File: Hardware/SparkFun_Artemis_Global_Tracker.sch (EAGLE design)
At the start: 144 parts, among them J1 IRIDIUM_9603N, J2 USB-C, J6 U.FL, J7 ANTENNA-GROUNDEDEDGE_SMA, J8 STANDOFFS_M2X0.4_STEEL_6MM, J9 STANDOFFS_M2X0.4_STEEL_6MM, Q1 5.8A/30V/35mΩ, Q2 20V/4.2A/52mΩ/1.4W, Q3 20V/4.2A/52mΩ/1.4W, Q4 600mA/40V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

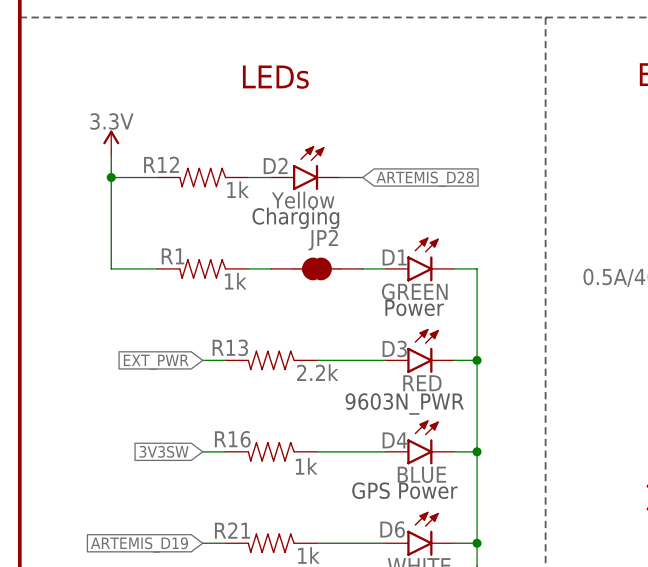
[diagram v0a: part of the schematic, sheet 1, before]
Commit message: silk updates and R1 to 330 for brighter green power led
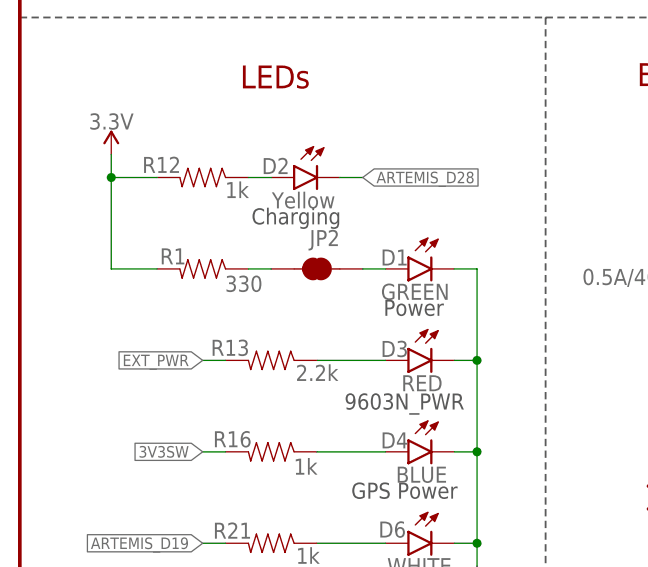
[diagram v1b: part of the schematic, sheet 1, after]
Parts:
- R1: value 1k -> 330; device SparkFun-Resistors:1KOHM-0603-1/10W-1% -> SparkFun-Resistors:330OHM-0603-1/10W-1%
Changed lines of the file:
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@@
 <part name="JP7" library="SparkFun-Aesthetics" deviceset="FIDUCIAL" device="1X2"/>
 <part name="JP13" library="SparkFun-Aesthetics" deviceset="FIDUCIAL" device="1X2"/>
-<part name="R1" library="SparkFun-Resistors" deviceset="1KOHM" device="-0603-1/10W-1%" value="1k"/>
+<part name="R1" library="SparkFun-Resistors" deviceset="330OHM" device="-0603-1/10W-1%" value="330"/>
 <part name="SUPPLY10" library="SparkFun-PowerSymbols" deviceset="3.3V" device=""/>
 <part name="D1" library="SparkFun-LED" deviceset="LED-GREEN" device="0603" value="GREEN"/>
@@
 <instance part="R1" gate="G$1" x="20.32" y="175.26" smashed="yes" rot="MR0">
 <attribute name="NAME" x="17.018" y="175.768" size="1.778" layer="95" font="vector" rot="MR0" align="bottom-center"/>
-<attribute name="VALUE" x="23.876" y="174.752" size="1.778" layer="96" font="vector" rot="MR0" align="top-center"/>
+<attribute name="VALUE" x="24.892" y="174.498" size="1.778" layer="96" font="vector" rot="MR0" align="top-center"/>
 </instance>
 <instance part="SUPPLY10" gate="G$1" x="10.16" y="187.96" smashed="yes" rot="MR0">

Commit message: backup battery charge resistor val and switch
-added pch mosfet to switch backup battery charging on and off via GPIO on artemis
-changed backup battery charge source to 3.3V rail, and changed charge resistor to 3.3K
-Moved Iridium module and artemis module down 0.1 inch to allow more clearance around sam-tech connector so epoxy is less likely to flow over/into nearby additional supercap pth pads.
-moved a few other components from 0603 to 0402 to make more room.
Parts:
- added Q6: 20V/4.2A/52mΩ/1.4W, SparkFun-DiscreteSemi:MOSFET_PCH-DMG2305UX-7
- added R19: 10K, SparkFun-Resistors:10KOHM-0402-1/10W-0.1%
- R1: device SparkFun-Resistors:330OHM-0603-1/10W-1% -> SparkFun-Resistors:330OHM-0402T-1/16W-5%
- R12, R16, R2, R21, R25, R29, R3: device SparkFun-Resistors:1KOHM-0603-1/10W-1% -> SparkFun-Resistors:1KOHM-0402T-1/16W-1%
- R13: value 2.2k -> 2.0K; device SparkFun-Resistors:2.2KOHM-0603-1/10W-1% -> SparkFun-Resistors:2.0KOHM-0402T-1/16W-1%
- R15: value 62KOHM-0603-1/10W-5% -> 3.3K; device SparkFun-Resistors:62KOHM-0603-1/10W-5% -> SparkFun-Resistors:3.3KOHM-0402T-1/16W-1%
- R28: value 2.0k -> 2.0K; device SparkFun-Resistors:2.0KOHM-0603-1/10W-5% -> SparkFun-Resistors:2.0KOHM-0402T-1/16W-1%
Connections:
- new net ARTEMIS_D44: Q6.G, R19.1, U7.(SDO4)~D44
- new net N$7: D5.A, Q6.D
- net 3.3V: now also Q6.S, R19.2
- net V_USB: no longer D5.A
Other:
- note added: "Back-Up Battery And charge control switch"
- note added: "R15 = (3.3 - (3.1 + 0.1)) / 30E-6 = ~3.3K"
- note removed: "Back-Up Battery"
- note removed: "R15 = (5 - (3.1 + 0.1)) / 30E-6 = ~60K"
- moved on the sheet: 3V3SW, B1, C12, C14, C15, C16, D5, J6, J7, Q2, R15, R17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

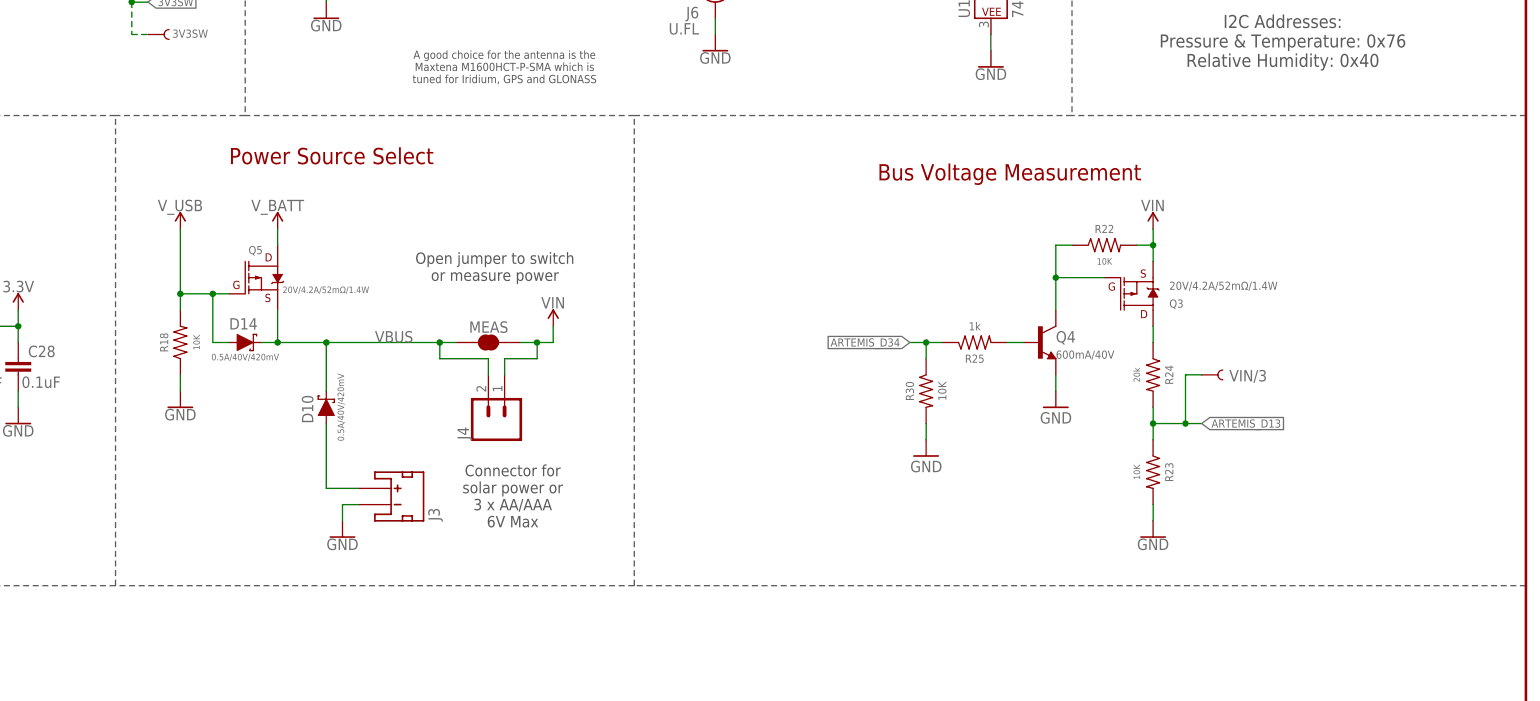
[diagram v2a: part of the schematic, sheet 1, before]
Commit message: Reverted back to battery input diode
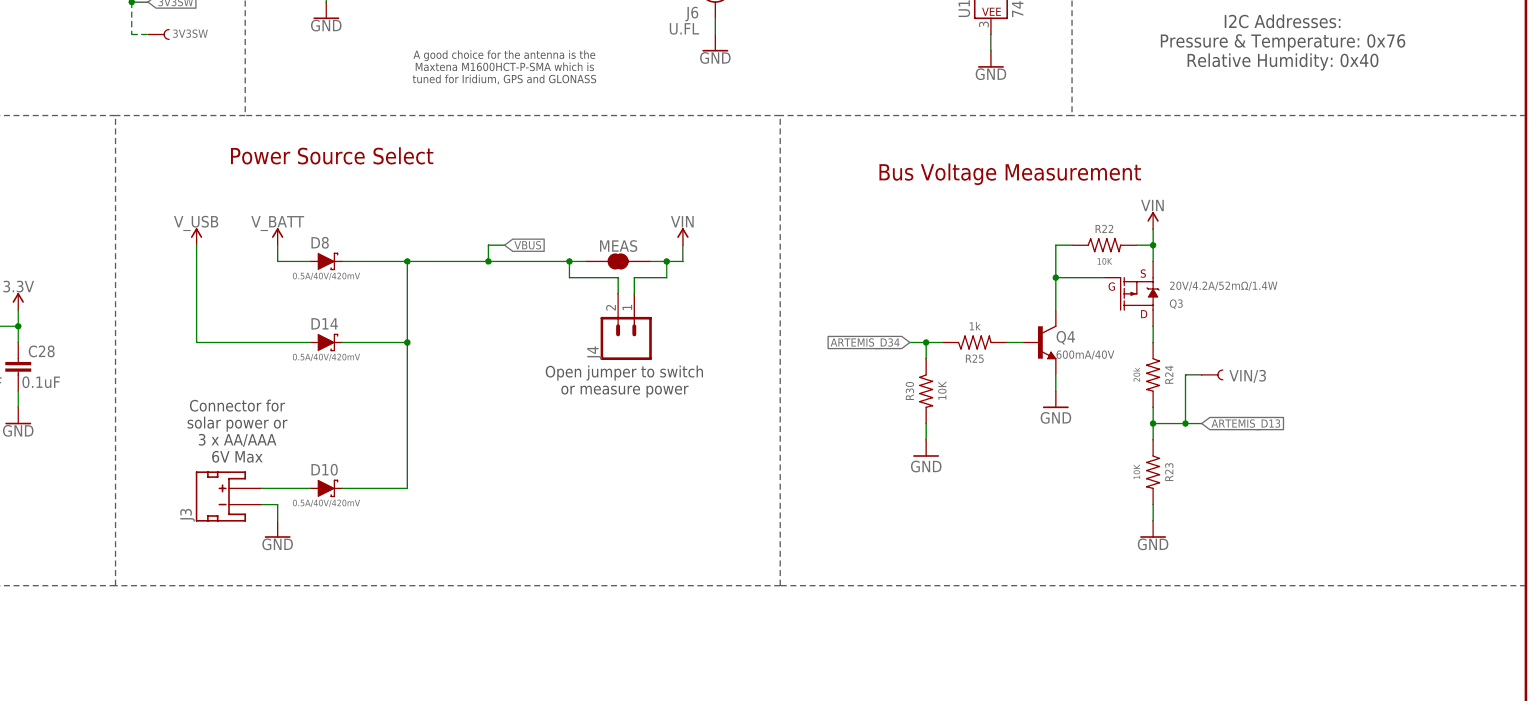
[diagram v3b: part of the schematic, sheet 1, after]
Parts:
- removed Q5: 20V/4.2A/52mΩ/1.4W, SparkFun-DiscreteSemi:MOSFET_PCH-DMG2305UX-7
- removed R18: 10K, SparkFun-Resistors:10KOHM-0402-1/10W-0.1%
- added D8: 0.5A/40V/420mV, SparkFun-DiscreteSemi:DIODE-SCHOTTKY-PMEG4005EJ
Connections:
- net GND: no longer R18.1
- net VBUS: now also D8.C; no longer Q5.S
- net V_BATT: now also D8.A; no longer Q5.D
- net V_USB: no longer Q5.G, R18.2
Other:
- moved on the sheet: D10, D14, J3, J4, MEAS

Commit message: Moved all 0.1uF caps to higher spec'd part
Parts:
- C13, C28, C7: device SparkFun-Capacitors:0.1UF-0402T-16V-10% -> SparkFun-Capacitors:0.1UF-0603-25V-5%
- C20: device SparkFun-Capacitors:0.1UF-0603-25V-(+80/-20%) -> SparkFun-Capacitors:0.1UF-0603-25V-5%
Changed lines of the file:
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@@
 <part name="B1" library="SparkFun-Batteries" deviceset="ML414H_IV01E_BATTERY" device=""/>
 <part name="L1" library="SparkFun-Coils" deviceset="2.2μH_SHIELDED_INDUCTOR" device="" value="2.2uH"/>
-<part name="C13" library="SparkFun-Capacitors" deviceset="0.1UF" device="-0402T-16V-10%" value="0.1uF"/>
+<part name="C13" library="SparkFun-Capacitors" deviceset="0.1UF" device="-0603-25V-5%" value="0.1uF"/>
 <part name="JP2" library="SparkFun-Jumpers" deviceset="JUMPER-SMT_2_NC_TRACE" device="_SILK" package3d_urn="urn:adsk.eagle:package:39281/1"/>
 <part name="SUPPLY20" library="SparkFun-PowerSymbols" deviceset="3.3V" device=""/>
@@
 <part name="C19" library="SparkFun-Capacitors" deviceset="15PF" device="-0603-50V-5%" value="15pF"/>
 <part name="GND35" library="SparkFun-PowerSymbols" deviceset="GND" device=""/>
-<part name="C20" library="SparkFun-Capacitors" deviceset="0.1UF" device="-0603-25V-(+80/-20%)" value="0.1uF"/>
+<part name="C20" library="SparkFun-Capacitors" deviceset="0.1UF" device="-0603-25V-5%" value="0.1uF"/>
 <part name="C22" library="SparkFun-Capacitors" deviceset="10UF" device="-0603-6.3V-20%" value="10uF"/>
 <part name="C23" library="SparkFun-Capacitors" deviceset="1.0UF" device="-0603-16V-10%" value="1.0uF"/>
@@
 <part name="C25" library="SparkFun-Capacitors" deviceset="22UF" device="-0603-6.3V-20%" value="22uF"/>
 <part name="C27" library="SparkFun-Capacitors" deviceset="1.0UF" device="-0603-16V-10%" value="1.0uF"/>
-<part name="C28" library="SparkFun-Capacitors" deviceset="0.1UF" device="-0402T-16V-10%" value="0.1uF"/>
+<part name="C28" library="SparkFun-Capacitors" deviceset="0.1UF" device="-0603-25V-5%" value="0.1uF"/>
 <part name="SUPPLY32" library="SparkFun-PowerSymbols" deviceset="3.3V" device=""/>
 <part name="R21" library="SparkFun-Resistors" deviceset="1KOHM" device="-0402T-1/16W-1%" value="1k"/>
@@
 <part name="D13" library="SparkFun-LED" deviceset="LED-YELLOW" device="0603" value="Yellow"/>
 <part name="R2" library="SparkFun-Resistors" deviceset="1KOHM" device="-0402T-1/16W-1%" value="1k"/>
-<part name="C7" library="SparkFun-Capacitors" deviceset="0.1UF" device="-0402T-16V-10%" value="0.1uF"/>
+<part name="C7" library="SparkFun-Capacitors" deviceset="0.1UF" device="-0603-25V-5%" value="0.1uF"/>
 <part name="R3" library="SparkFun-Resistors" deviceset="1KOHM" device="-0402T-1/16W-1%" value="1k"/>
 <part name="D7" library="SparkFun-LED" deviceset="LED-GREEN" device="0603" value="GREEN"/>

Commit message: Moved all 1.0uF caps to higher spec'd part
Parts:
- C23, C24, C27: device SparkFun-Capacitors:1.0UF-0603-16V-10% -> SparkFun-Capacitors:1.0UF-0603-16V-10%-X7R
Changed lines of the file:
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@@
 <part name="C20" library="SparkFun-Capacitors" deviceset="0.1UF" device="-0603-25V-5%" value="0.1uF"/>
 <part name="C22" library="SparkFun-Capacitors" deviceset="10UF" device="-0603-6.3V-20%" value="10uF"/>
-<part name="C23" library="SparkFun-Capacitors" deviceset="1.0UF" device="-0603-16V-10%" value="1.0uF"/>
+<part name="C23" library="SparkFun-Capacitors" deviceset="1.0UF" device="-0603-16V-10%-X7R" value="1.0uF"/>
 <part name="SUPPLY9" library="SparkFun-PowerSymbols" deviceset="3.3V" device=""/>
 <part name="SUPPLY21" library="SparkFun-PowerSymbols" deviceset="3.3V" device=""/>
@@
 <part name="C21" library="SparkFun-Capacitors" deviceset="22UF" device="-0805-16V-20%" value="22uF"/>
 <part name="C25" library="SparkFun-Capacitors" deviceset="22UF" device="-0603-6.3V-20%" value="22uF"/>
-<part name="C27" library="SparkFun-Capacitors" deviceset="1.0UF" device="-0603-16V-10%" value="1.0uF"/>
+<part name="C27" library="SparkFun-Capacitors" deviceset="1.0UF" device="-0603-16V-10%-X7R" value="1.0uF"/>
 <part name="C28" library="SparkFun-Capacitors" deviceset="0.1UF" device="-0603-25V-5%" value="0.1uF"/>
 <part name="SUPPLY32" library="SparkFun-PowerSymbols" deviceset="3.3V" device=""/>
@@
 <part name="JP10" library="SparkFun-Hardware" deviceset="STAND-OFF" device=""/>
 <part name="JP9" library="SparkFun-Hardware" deviceset="STAND-OFF" device=""/>
-<part name="C24" library="SparkFun-Capacitors" deviceset="1.0UF" device="-0603-16V-10%" value="1.0uF"/>
+<part name="C24" library="SparkFun-Capacitors" deviceset="1.0UF" device="-0603-16V-10%-X7R" value="1.0uF"/>
 <part name="SUPPLY17" library="SparkFun-PowerSymbols" deviceset="3.3V" device=""/>
 <part name="GND37" library="SparkFun-PowerSymbols" deviceset="GND" device=""/>

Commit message: Moved C25 to 0805 higher voltage rating
-to decrease BOM diversity
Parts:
- C25: device SparkFun-Capacitors:22UF-0603-6.3V-20% -> SparkFun-Capacitors:22UF-0805-16V-20%
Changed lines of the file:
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@@
 <part name="U7" library="SparkFun-IC-Microcontroller" deviceset="ARTEMIS_MODULE" device="SMD"/>
 <part name="C21" library="SparkFun-Capacitors" deviceset="22UF" device="-0805-16V-20%" value="22uF"/>
-<part name="C25" library="SparkFun-Capacitors" deviceset="22UF" device="-0603-6.3V-20%" value="22uF"/>
+<part name="C25" library="SparkFun-Capacitors" deviceset="22UF" device="-0805-16V-20%" value="22uF"/>
 <part name="C27" library="SparkFun-Capacitors" deviceset="1.0UF" device="-0603-16V-10%-X7R" value="1.0uF"/>
 <part name="C28" library="SparkFun-Capacitors" deviceset="0.1UF" device="-0603-25V-5%" value="0.1uF"/>

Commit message: Routed 8 more Artemis GPIOs to PTH headers
-routed AD32, D43, D42, AD31, AD29, AD11, D15 and AD12 to 0.1" PTH headers on upper right edge of board.
-removed full size sparkfun logo, added large flame.
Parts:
- added J10, J11: (no value), SparkFun-Connectors:CONN_041X04_NO_SILK_NO_POP
- LOGO2: value SFE_LOGO_NAME_FLAME.1_INCH -> SFE_LOGO_FLAME.3_INCH; device SparkFun-Aesthetics:SFE_LOGO_NAME_FLAME.1_INCH -> SparkFun-Aesthetics:SFE_LOGO_FLAME.3_INCH
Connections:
- new net ARTEMIS_AD11: J11.3, U7.~AD11(PDMDATA)
- new net ARTEMIS_AD12: J11.1, U7.~AD12(PDMCLK/TX1)
- new net ARTEMIS_AD29: J11.4, U7.~AD29(PDMDATA)
- new net ARTEMIS_AD31: J10.1, U7.~AD31(SCCCLK)
- new net ARTEMIS_AD32: J10.4, U7.~AD32(SCCIO)
- new net ARTEMIS_D15: J11.2, U7.(ADCD1N/RX1/PDMDATA)D15
- new net ARTEMIS_D42: J10.2, U7.(SCL3/SCK3/TX1)~D42
- new net ARTEMIS_D43: J10.3, U7.(SDA3/SDI3/RX1)~D43
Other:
- moved on the sheet: C18, C19, C24, I2C, QWIIC, X1

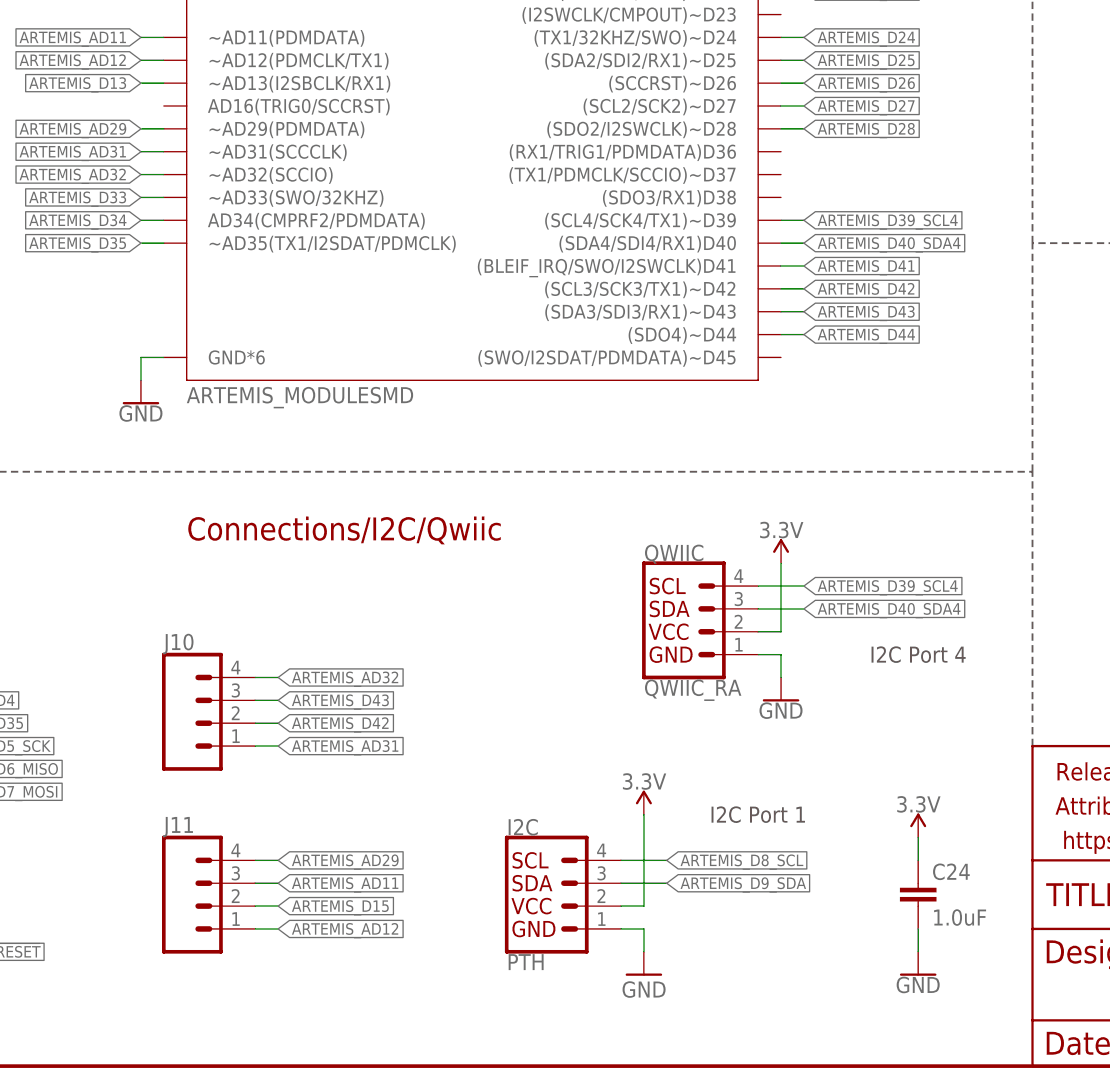
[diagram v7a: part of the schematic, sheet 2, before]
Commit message: Broke out D37 to bottom right corner PTH header
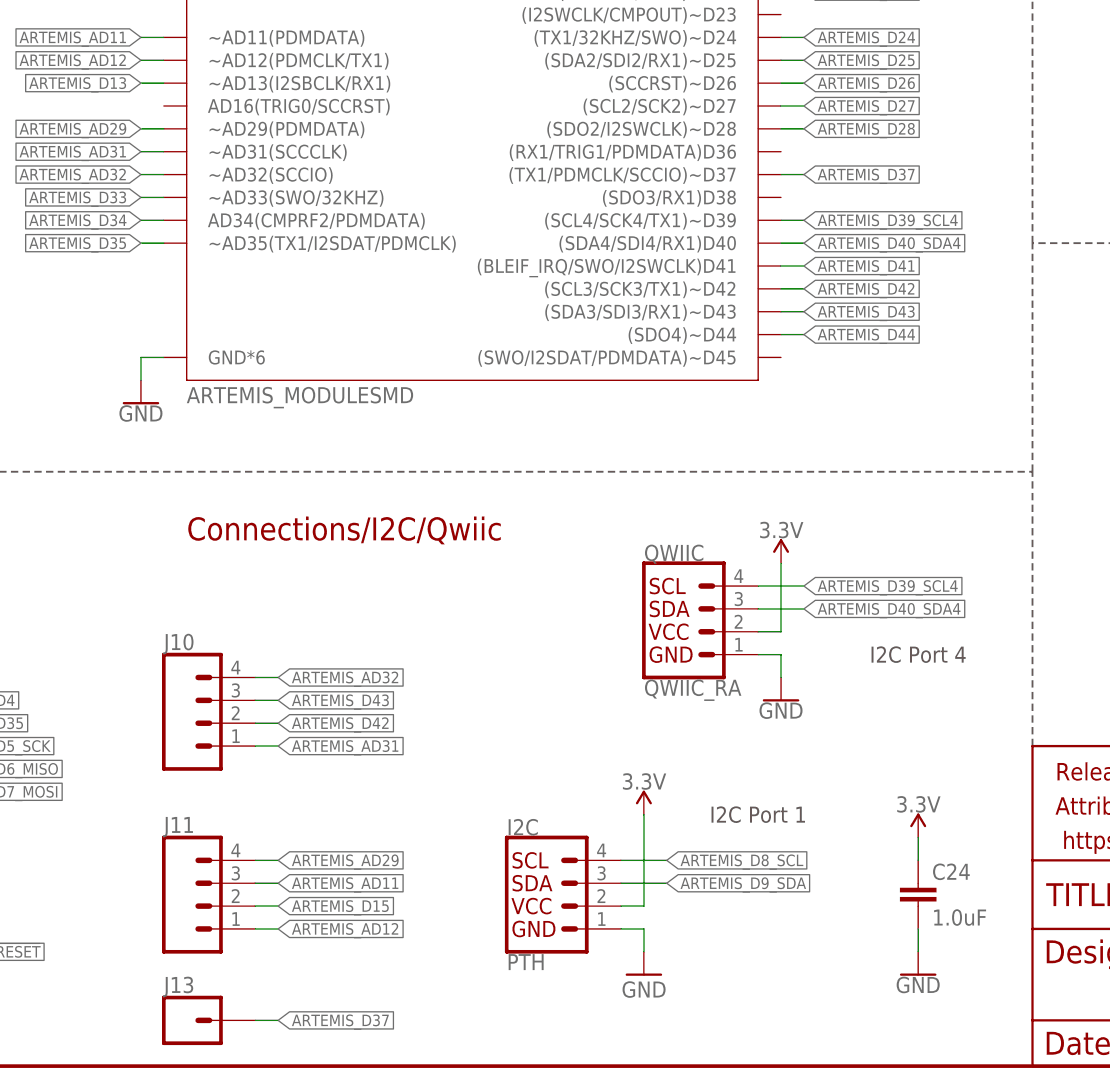
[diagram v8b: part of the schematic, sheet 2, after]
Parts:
- added J13: (no value), SparkFun-Connectors:CONN_01PTH_NO_SILK_YES_STOP
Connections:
- new net ARTEMIS_D37: J13.1, U7.(TX1/PDMCLK/SCCIO)~D37
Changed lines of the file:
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@@
 <part name="J11" library="SparkFun-Connectors" deviceset="CONN_04" device="1X04_NO_SILK_NO_POP"/>
 <part name="LOGO2" library="SparkFun-Aesthetics" deviceset="SFE_LOGO_FLAME" device=".3_INCH" value="SFE_LOGO_FLAME.3_INCH"/>
+<part name="J13" library="SparkFun-Connectors" deviceset="CONN_01" device="PTH_NO_SILK_YES_STOP"/>
 </parts>
 <sheets>
@@
 <attribute name="NAME" x="50.8" y="25.908" size="1.778" layer="95" font="vector"/>
 </instance>
+<instance part="J13" gate="G$1" x="53.34" y="5.08" smashed="yes">
+<attribute name="VALUE" x="50.8" y="0.254" size="1.778" layer="96" font="vector"/>
+<attribute name="NAME" x="50.8" y="8.128" size="1.778" layer="95" font="vector"/>
+</instance>
 </instances>
 <busses>
@@
 </segment>
 </net>
+<net name="ARTEMIS_D37" class="0">
+<segment>
+<pinref part="U7" gate="U1" pin="(TX1/PDMCLK/SCCIO)~D37"/>
+<wire x1="119.38" y1="99.06" x2="121.92" y2="99.06" width="0.1524" layer="91"/>
+<label x="121.92" y="99.06" size="1.27" layer="95" font="vector" xref="yes"/>
+</segment>
+<segment>
+<pinref part="J13" gate="G$1" pin="1"/>
+<wire x1="60.96" y1="5.08" x2="63.5" y2="5.08" width="0.1524" layer="91"/>
+<label x="63.5" y="5.08" size="1.27" layer="95" font="vector" xref="yes"/>
+</segment>
+</net>
